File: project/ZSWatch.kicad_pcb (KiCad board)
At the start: 4 copper layers, 41 x 38 mm, 74 parts, among them IC1 APDS-9306-065, IC10 FAN5622SX, IC11 XC9265A331MR-G, IC12 BMP581, IC13 BME688, IC14 LIS2MDLTR, IC15 DRV2603RUNT, IC2 ESDALC6V1W5, IC3 MAX1811ESA+, IC4 DMC2400UV-7, IC5 NCV300LSN36T1G, IC6 AT25SL128A, IC7 XC9265C181MR-G, IC8 BMI270, IC9 NTS0104GU12, M1 NORA-B106, X1 DOCK, X10 M-, X2 BATTERY, X3 GPIO0, X4 GPIO1, X5 GPIO2, X6 GPIO3, X7 GND, X8 GC9A01A_CST816S, X9 M+

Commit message: - Change PCB thickness to 1 mm
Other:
- board text added: "0,11 mm"
- board text added: "0,6 mm"
- board text added: "0,9800 mm"
- board text added: "Dielektrikum"
- board text removed: "0,48 mm"
- board text removed: "1,6000 mm"
- board text removed: "Dielektrikum 1"
- board text removed: "Dielektrikum 2"
- board text removed: "Dielektrikum 3"

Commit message: - Add blue color to PCB settings - Add surface option to PCB settings
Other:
- board text added: "HAL lead-free"
- board text removed: "None"

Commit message: - Streamline documentation and production files - Ready to merge
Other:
- board text added: "Blue"
- board text added: "Dielektrikum 1"
- board text added: "Dielektrikum 2"
- board text added: "Dielektrikum 3"
- board text added: "FR4 natural"
- board text added: "HAL SnPb"
- board text added: "White"
- board text removed: "Dielektrikum"
- board text removed: "HAL lead-free"

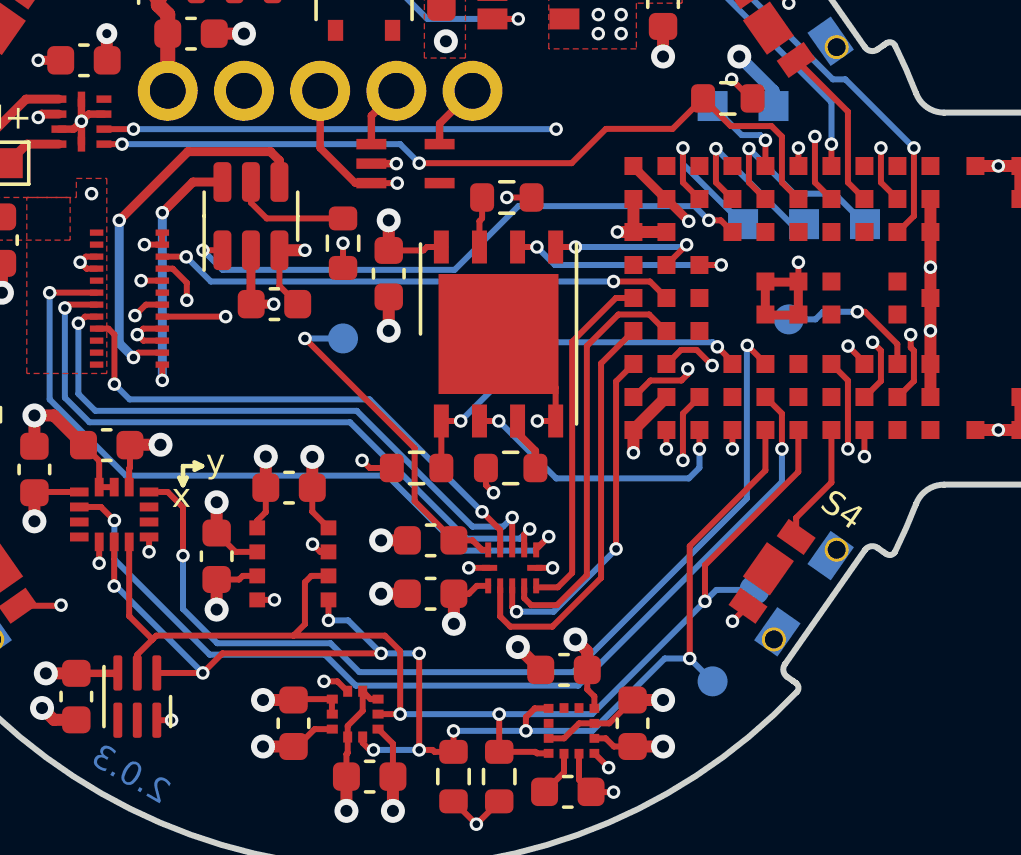
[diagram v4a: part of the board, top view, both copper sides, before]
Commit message: Use QSPI for flash.
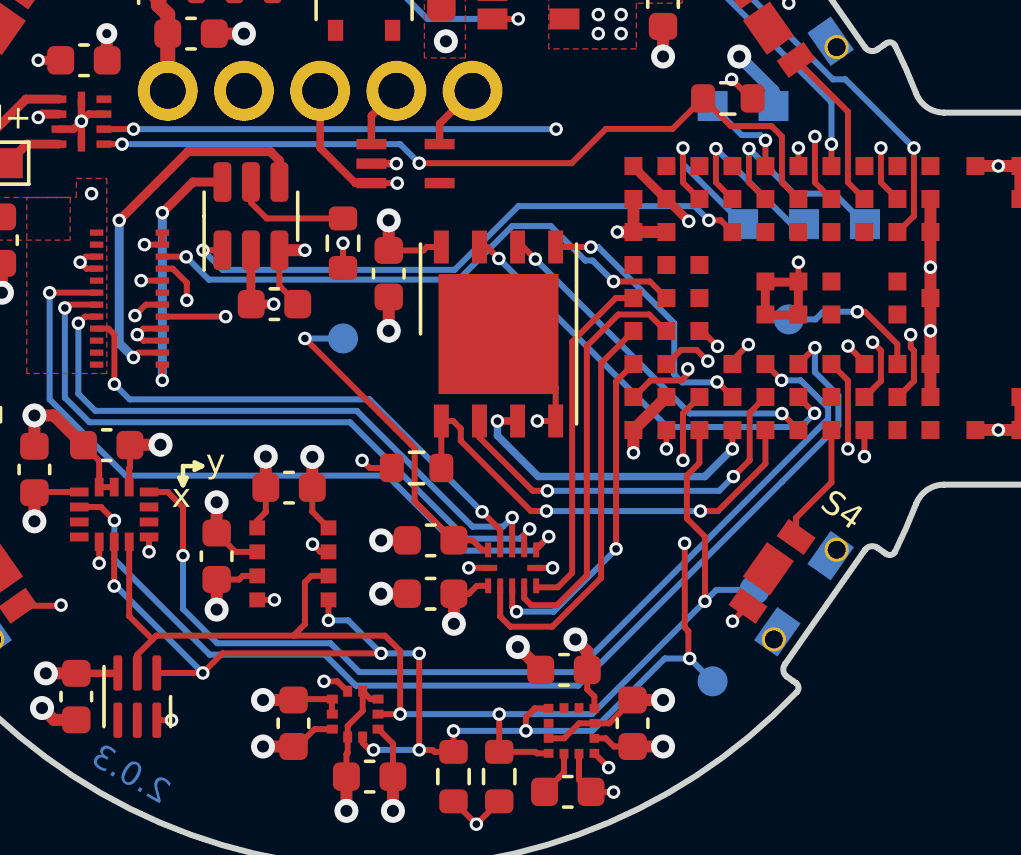
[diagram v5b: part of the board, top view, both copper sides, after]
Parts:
- removed R10, R4: 100k, Resistor_SMD:R_0603_1608Metric
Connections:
- IC6 pad 1: FLASH_CS -> QSPI_CS
- IC6 pad 2: FLASH_SO -> QSPI_IO1
- IC6 pad 3: Net-(IC6-~{WP(I}/O2)) -> QSPI_IO2
- IC6 pad 5: FLASH_SI -> QSPI_IO0
- IC6 pad 6: FLASH_CLK -> QSPI_CLK
- IC6 pad 7: Net-(IC6-~{HOLD(I}/O3)) -> QSPI_IO3
- M1 pad B6: FLASH_SI -> unconnected-(M1B-P0.01/XL2-PadB6)
- M1 pad C1: FLASH_SO -> SENSOR_SDA
- M1 pad C4: unconnected-(M1C-P1.01-PadC4) -> DISPLAY_EN
- M1 pad C6: FLASH_CLK -> unconnected-(M1B-P0.00/XL1-PadC6)
- M1 pad D1: DISPLAY_EN -> QSPI_IO2
- M1 pad D2: unconnected-(M1B-P0.13/QSPI[0]-PadD2) -> QSPI_IO0
- M1 pad D3: FLASH_CS -> SENSOR_SCL
- M1 pad E1: SENSOR_SCL -> QSPI_CS
- M1 pad E2: INT2_LIS -> QSPI_IO1
- M1 pad F1: SENSOR_SDA -> QSPI_CLK
- M1 pad F2: unconnected-(M1B-P0.16/QSPI[3]-PadF2) -> QSPI_IO3
- M1 pad F3: unconnected-(M1B-P0.19-PadF3) -> INT2_LIS
- R6 pad 2: FLASH_CS -> QSPI_CS
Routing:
- net QSPI_CS: track 0.00 -> 15.6 mm, vias 0 -> 2
- net QSPI_IO3: track 0.00 -> 14.6 mm, vias 0 -> 2
- net QSPI_IO1: track 0.00 -> 12.7 mm, vias 0 -> 2
- net FLASH_CS: track 12.7 -> 0.00 mm, vias 2 -> 0
- net QSPI_CLK: track 0.00 -> 11.9 mm, vias 0 -> 2
- net QSPI_IO2: track 0.00 -> 10.6 mm, vias 0 -> 2
- net FLASH_SO: track 9.50 -> 0.00 mm, vias 2 -> 0
- net QSPI_IO0: track 0.00 -> 8.98 mm, vias 0 -> 2
- net FLASH_CLK: track 7.64 -> 0.00 mm, vias 2 -> 0
- net FLASH_SI: track 5.22 -> 0.00 mm, vias 2 -> 0
- net SENSOR_SCL: track 44.8 -> 48.5 mm, vias 10 -> 12
- net DISPLAY_EN: track 34.1 -> 37.5 mm
- net INT2_LIS: track 32.5 -> 35.8 mm
- net Net-(IC6-~{WP(I}/O2)): track 1.81 -> 0.00 mm
- net +1V8: track 42.5 -> 40.7 mm, vias 24 -> 22
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
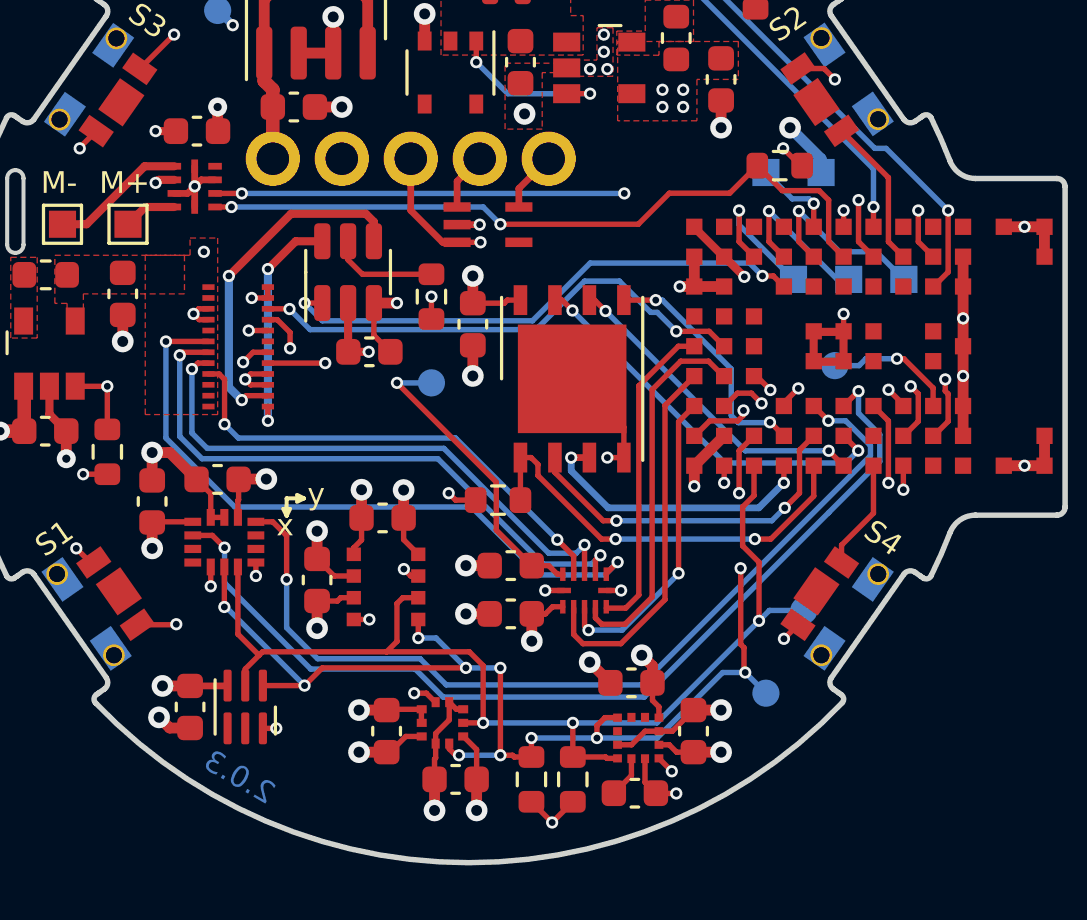
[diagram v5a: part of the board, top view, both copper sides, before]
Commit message: - Update libraries to the latest version - Set correct version number in CHANGELOG - Cosmetic changes - Add new production files
Signed-off-by: Daniel Kampert <DanielKampert@kampis-elektroecke.de>
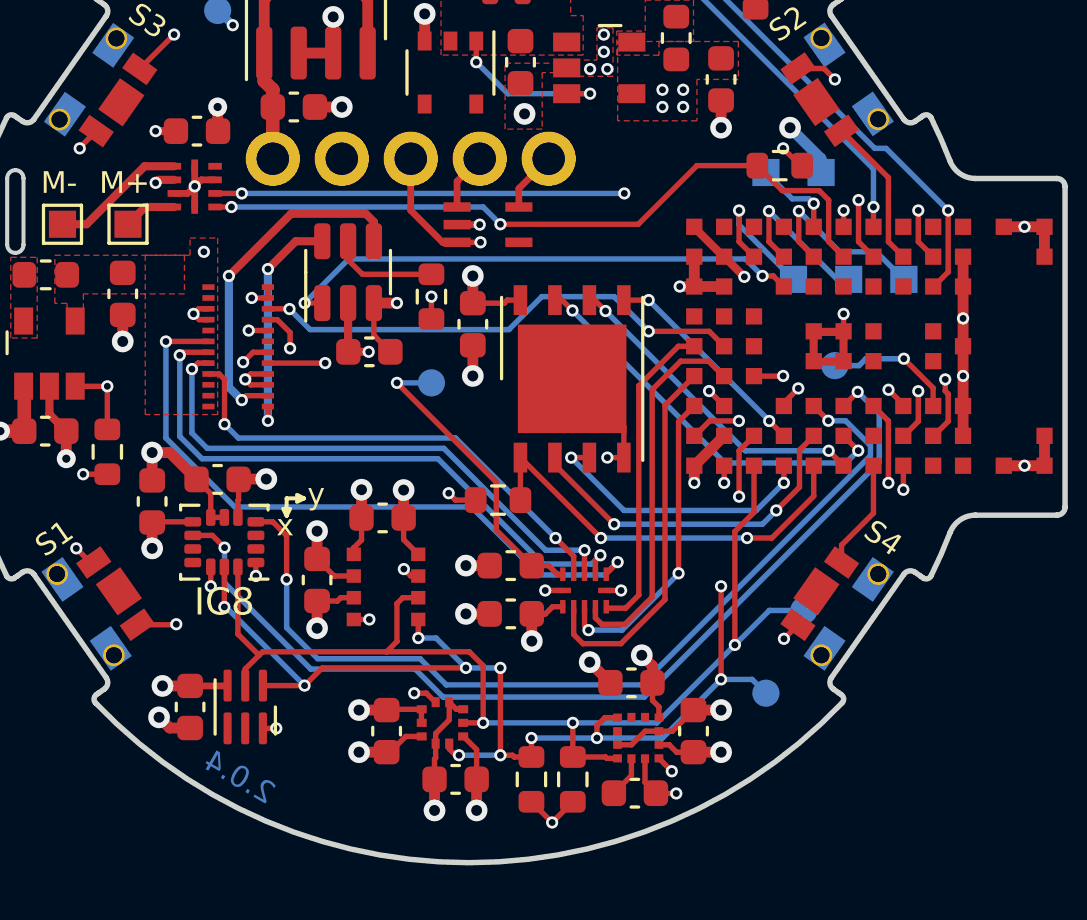
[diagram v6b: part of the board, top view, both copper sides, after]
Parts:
- IC8: footprint Package_LGA_Kampi:LGA-14_3x2.5mm_P0.5mm_LayoutBorder3x4y -> Package_LGA:LGA-14_3x2.5mm_P0.5mm_LayoutBorder3x4y
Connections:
- M1 pad A2: DISPLAY_DC -> DISPLAY_CS
- M1 pad B3: DISPLAY_CS -> DISPLAY_DC
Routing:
- net DISPLAY_DC: track 20.6 -> 17.9 mm
- net DISPLAY_CS: track 22.3 -> 21.1 mm
- net QSPI_IO0: track 8.98 -> 7.98 mm
- net SENSOR_SDA: track 41.7 -> 42.4 mm
- net DISPLAY_EN: track 37.5 -> 38.1 mm
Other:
- board text added: "2.0.${REVISION}"
- board text removed: "2.0.3"

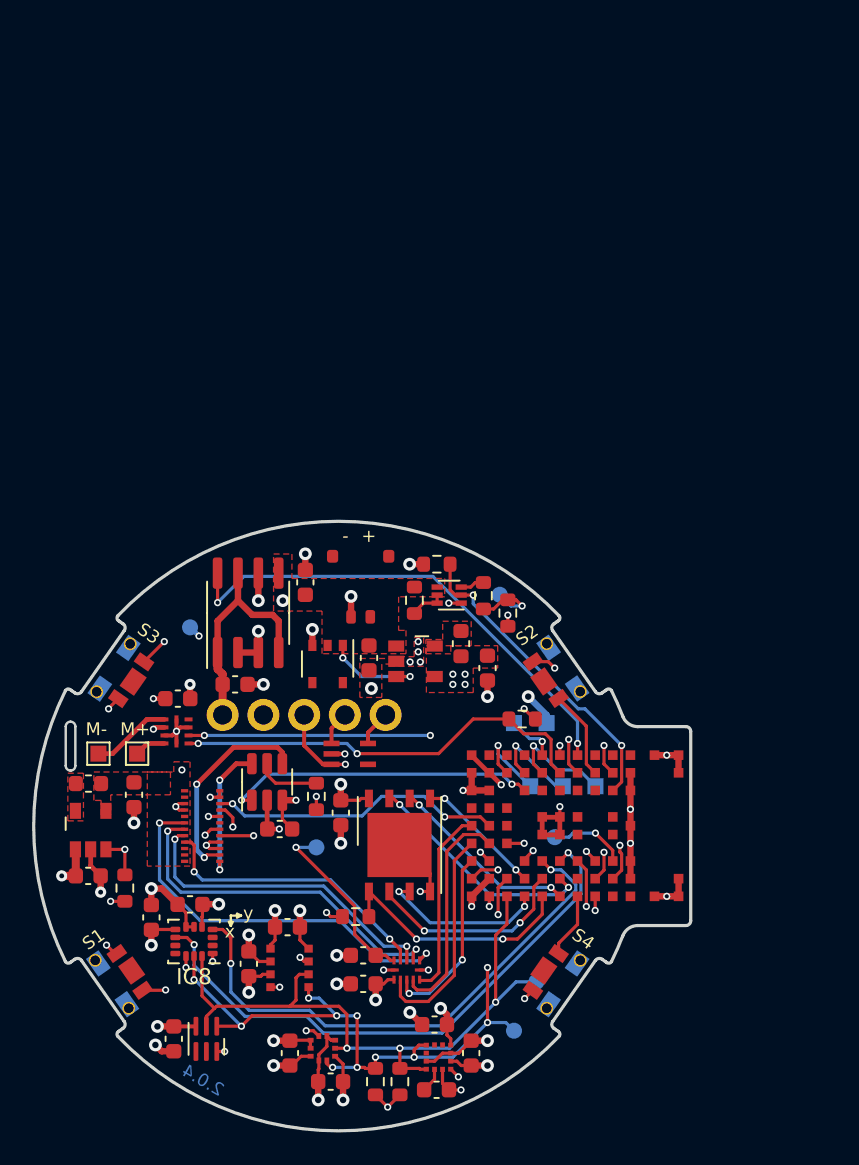
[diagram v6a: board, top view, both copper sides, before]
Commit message: - Add QR code library with link to the project - Change ISET resistor to 12k - Replace light sensor footprint with a version from our KiCad library - Rename the inner copper layers - Add KiBot file for production file generation - Import nPM1300 from test project - Remove pull down resistor from vibration driver IC enable - Split schematics into hierarical schematics - Add PCB variant for reduced sensor board
Signed-off-by: Daniel Kampert <DanielKampert@kampis-elektroecke.de>
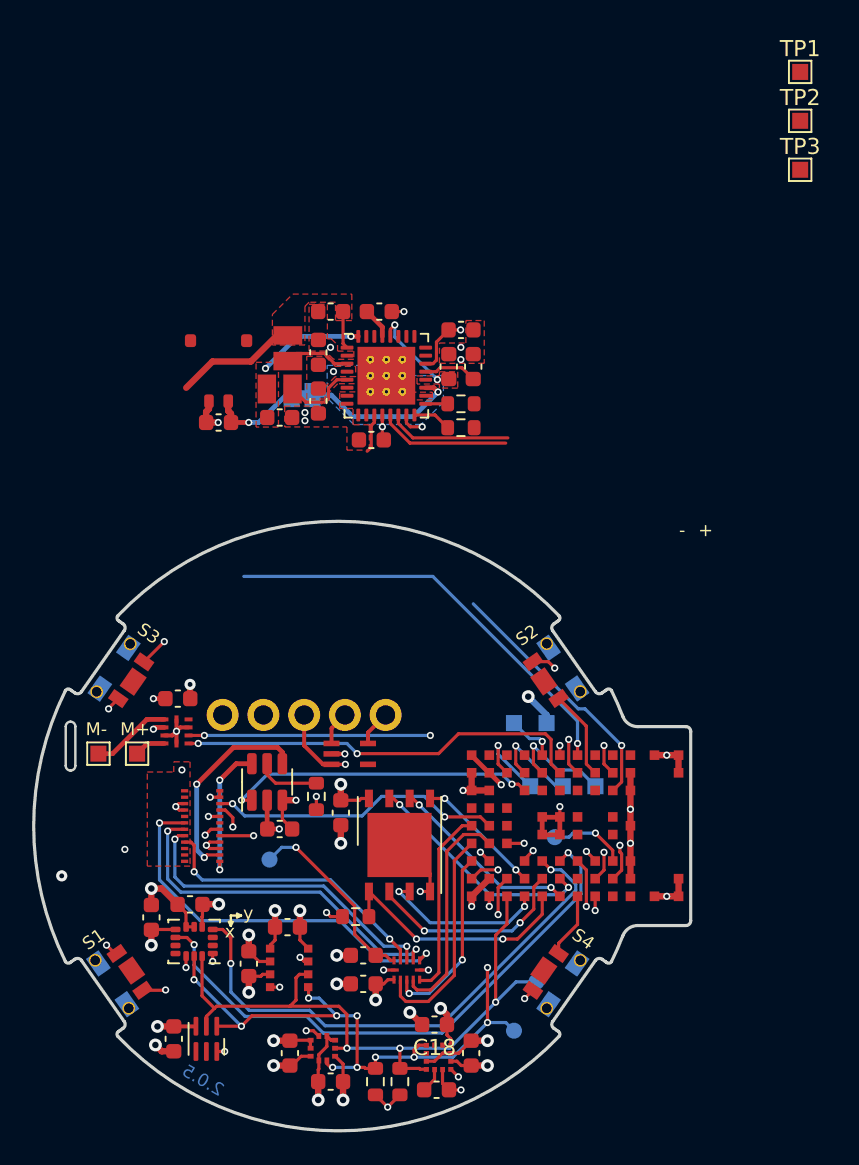
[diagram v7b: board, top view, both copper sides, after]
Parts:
- removed the C11 at (143.8, 115.8)
- removed the C14 at (146.6, 110.8)
- removed the C21 at (167.6, 126.9)
- removed the IC11 at (143.9, 113.0)
- removed IC12: BMP581, Package_LGA_Kampi:Bosch_LGA-10_2x2mm_P0.5mm_ClockwisePinNumbering
- removed IC13: BME688, Package_LGA_Kampi:Bosch_LGA-8_3x3mm_P0.8mm_ClockwisePinNumbering
- removed IC14: LIS2MDLTR, Package_LGA_Kampi:LGA-12_2x2mm_P0.5mm
- removed the IC7 at (164.2, 102.4)
- removed the IC8 at (150.4, 119.9)
- removed R11, R9: 100k, Resistor_SMD:R_0603_1608Metric
- removed the R3 at (169.9, 99.4)
- removed the R5 at (165.5, 96.4)
- removed the TP5 at (169.4, 98.3)
- removed the TP6 at (150.1, 100.3)
- removed the X2 at (160.8, 97.8)
- added C1: 1u, Capacitor_SMD:C_0603_1608Metric, F.Cu at (167.8, 84.1)
- added C10: 1u, Capacitor_SMD:C_0603_1608Metric, F.Cu at (167.0, 81.8)
- added C17: 100n, Capacitor_SMD:C_0603_1608Metric, F.Cu at (153.8, 121.3)
- added C5: 10u, Capacitor_SMD:C_0603_1608Metric, F.Cu at (155.7, 87.2)
- added C7: 10u, Capacitor_SMD:C_0603_1608Metric, F.Cu at (158.9, 80.6)
- added C8: 10u, Capacitor_SMD:C_0603_1608Metric, F.Cu at (161.9, 80.6)
- added C9: 10u, Capacitor_SMD:C_0603_1608Metric, F.Cu at (166.2, 84.1)
- added G***: LOGO, project:QR-Code, B.Cu at (159.6, 98.3)
- added IC1: nPM1300-QEXX, Package_DFN_QFN:QFN-32-1EP_5x5mm_P0.5mm_EP3.6x3.6mm_ThermalVias, F.Cu at (162.4, 84.6)
- added IC6: LIS2MDLTR, Package_LGA_Kampi:LGA-12_2x2mm_P0.5mm, F.Cu at (165.6, 127.1)
- added J1: ~, Jumper:SolderJumper-2_P1.3mm_Bridged_Pad1.0x1.5mm, B.Cu at (157.1, 85.9)
- added TP1: 3V3, TestPoint:TestPoint_Pad_1.0x1.0mm, F.Cu at (188.1, 65.7)
- added TP2: 1V8, TestPoint:TestPoint_Pad_1.0x1.0mm, F.Cu at (188.1, 68.8)
- added TP3: 3V0, TestPoint:TestPoint_Pad_1.0x1.0mm, F.Cu at (188.1, 71.8)
- added X1: BATTERY, Molex:78171-0002, F.Cu at (151.9, 84.4)
- added kibuzzard-656642B5: G***, kibuzzard-656642B5, B.Cu at (152.0, 110.5)
- added kibuzzard-656642E4: G***, kibuzzard-656642E4, B.Cu at (154.7, 110.9)
- added kibuzzard-65664307: G***, kibuzzard-65664307, B.Cu at (157.2, 111.6)
- added kibuzzard-65664337: G***, kibuzzard-65664337, B.Cu at (159.8, 111.6)
- added kibuzzard-65664342: G***, kibuzzard-65664342, B.Cu at (162.3, 111.6)
- C2: value 4u7 -> 100n
- C6: value 22u -> 10u
- IC2: renamed from IC1; footprint OptoDevice:Broadcom_DFN-6_2x2mm_P0.65mm -> Broadcom:Broadcom_DFN-6_2x2mm_P0.65mm
- IC3: value MAX1811ESA+ -> BMI270; footprint Package_SO:SOIC-8_3.9x4.9mm_P1.27mm -> Package_LGA:LGA-14_3x2.5mm_P0.5mm_LayoutBorder3x4y
- IC4: value DMC2400UV-7 -> BMP581; footprint Package_TO_SOT_SMD:SOT-563 -> Package_LGA_Kampi:Bosch_LGA-10_2x2mm_P0.5mm_ClockwisePinNumbering
- IC5: value NCV300LSN36T1G -> BME688; footprint Package_SO:TSOP-5_1.65x3.05mm_P0.95mm -> Package_LGA_Kampi:Bosch_LGA-8_3x3mm_P0.8mm_ClockwisePinNumbering
- L1, L2: value 10u -> 2u2; footprint Inductor_SMD:L_0603_1608Metric -> Inductor_SMD_Kampi:L_0806_2016
- R1: value 1M -> 47k
- R2: value 1M5 / 0.1% -> 150k
- R7: renamed from R12; value 10k -> 12k
- moved L2 29.8 mm to (156.2, 82.9), turned to -90 degrees
- moved IC4 29.3 mm to (158.4, 126.6)
- moved IC3 20.8 mm to (150.4, 119.9), turned to 180 degrees
- moved C6 19.7 mm to (158.1, 86.2)
- moved L1 19.5 mm to (155.7, 85.5), turned to 0 degrees
- moved C4 19.3 mm to (158.1, 83.2), turned to 90 degrees
- moved IC5 19.1 mm to (156.3, 121.6)
- moved C2 17.4 mm to (161.4, 88.6), turned to 180 degrees
- moved C20 14.9 mm to (167.6, 126.9), turned to -90 degrees
- moved R1 12.6 mm to (167.0, 86.4), turned to 180 degrees
- moved C3 11.3 mm to (151.9, 87.6), turned to 180 degrees
- moved R2 10.6 mm to (167.0, 87.9), turned to 180 degrees
- moved TP7 3.02 mm to (155.1, 114.8)
- renumbered C7 to C11, C1 to C12, C8 to C13, C13 to C14, C17 to C20, C5 to C21, C20 to C22, C9 to C23, C10 to C24, C12 to C25, IC9 to IC10, IC10 to IC11, IC2 to IC7, IC6 to IC8, IC15 to IC9, R6 to R3, R7 to R4, R8 to R5, TP1 to TP4, TP2 to TP5, TP3 to TP6, TP4 to TP7, X8 to X10, X1 to X2, X9 to X8, X10 to X9
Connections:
- C2 pad 1: VBUS -> +1V8
- C3 pad 1: GND -> Net-(J1-A)
- C3 pad 2: +BATT -> GND
- C4 pad 1: +BATT -> VSYS
- C6 pad 1: +1V8 -> VSYS
- IC2 pad 1: SENSOR_SCL -> /MCU/SENSOR-SCL
- IC2 pad 2: SENSOR_SDA -> /MCU/SENSOR-SDA
- IC3 pad 1: VBUS -> GND
- IC3 pad 2: GND -> unconnected-(IC3-ASDX-Pad2)
- IC3 pad 3: GND -> unconnected-(IC3-ASCX-Pad3)
- IC3 pad 4: VBUS -> /MCU/LIS-INT1
- IC3 pad 5: +BATT -> +1V8
- IC3 pad 7: VBUS -> GND
- IC3 pad 8: CHG -> +1V8
- IC4 pad 1: GND -> +1V8
- IC4 pad 2: BAT_MON_EN -> /MCU/SENSOR-SCL
- IC4 pad 3: Net-(IC4-D2) -> GND
- IC4 pad 4: +BATT -> /MCU/SENSOR-SDA
- IC4 pad 5: Net-(IC4-D1) -> +1V8
- IC4 pad 6: Net-(IC4-D1) -> +1V8
- IC5 pad 1: Net-(IC5-~{RESET}) -> GND
- IC5 pad 2: +BATT -> +1V8
- IC5 pad 3: GND -> /MCU/SENSOR-SDA
- IC5 pad 4: (no net) -> /MCU/SENSOR-SCL
- IC5 pad 5: (no net) -> GND
- L1 pad 1: Net-(IC7-LX) -> +3V0
- L1 pad 2: +1V8 -> Net-(IC1-SW2)
- L2 pad 1: Net-(IC11-LX) -> +1V8
- L2 pad 2: DISPLAY_3V3 -> Net-(IC1-SW1)
- M1 pad B9: unconnected-(M1A-VBUS-PadB9) -> VBUS
- M1 pad C1: SENSOR_SDA -> /MCU/SENSOR-SDA
- M1 pad D3: SENSOR_SCL -> /MCU/SENSOR-SCL
- M1 pad E3: INT1_LIS -> /MCU/LIS-INT1
- M1 pad F3: INT2_LIS -> /MCU/LIS-INT2
- M1 pad G3: BMP581_INT -> /MCU/BMP581_INT
- M1 pad G9: CHG -> unconnected-(M1C-P1.13-PadG9)
- M1 pad H1: LIS2MDL_INT -> /MCU/LIS2MDL_INT
- M1 pad J7: BAT_MON_EN -> unconnected-(M1C-P1.10-PadJ7)
- M1 pad J8: BAT_MON -> unconnected-(M1B-P0.28/AIN7-PadJ8)
- R1 pad 1: +BATT -> GND
- R1 pad 2: Net-(IC4-D1) -> Net-(IC1-VSET1)
- R2 pad 1: Net-(IC4-D2) -> GND
- R2 pad 2: BAT_MON -> Net-(IC1-VSET2)
- R4 pad 1: SENSOR_SCL -> /MCU/SENSOR-SCL
- R5 pad 1: SENSOR_SDA -> /MCU/SENSOR-SDA
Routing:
- net /MCU/SENSOR-SCL: track 0.00 -> 56.5 mm, vias 0 -> 12
- net /MCU/SENSOR-SDA: track 0.00 -> 50.6 mm, vias 0 -> 3
- net SENSOR_SCL: track 48.7 -> 0.00 mm, vias 12 -> 0
- net SENSOR_SDA: track 42.4 -> 0.00 mm, vias 3 -> 0
- net INT2_LIS: track 35.7 -> 0.00 mm, vias 2 -> 0
- net /MCU/LIS-INT2: track 0.00 -> 35.7 mm, vias 0 -> 2
- net INT1_LIS: track 33.3 -> 0.00 mm, vias 2 -> 0
- net /MCU/LIS-INT1: track 0.00 -> 33.3 mm, vias 0 -> 2
- net CHG: track 30.8 -> 0.00 mm, vias 2 -> 0
- net unconnected-(M1C-P1.13-PadG9): track 0.00 -> 26.7 mm, vias 0 -> 1
- net BMP581_INT: track 24.7 -> 0.00 mm, vias 2 -> 0
- net /MCU/BMP581_INT: track 0.00 -> 24.7 mm, vias 0 -> 2
- net BAT_MON_EN: track 19.7 -> 0.00 mm, vias 2 -> 0
- net BAT_MON: track 17.2 -> 0.00 mm, vias 2 -> 0
- net LIS2MDL_INT: track 16.2 -> 0.00 mm, vias 2 -> 0
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- added copper zone on F.Cu, net +3V0
- added copper zone on B.Cu, net VSYS
- added copper zone on F.Cu, net VSYS
- removed copper zone on F.Cu, net +BATT
- removed copper zone on F.Cu, net Net-(IC11-LX)
- removed copper zone on F.Cu, net Net-(IC7-LX)
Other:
- board text removed: "5V"
- board text removed: "GND"
- board text removed: "Reset"
- board text removed: "SWDCLK"
- board text removed: "SWDIO"
